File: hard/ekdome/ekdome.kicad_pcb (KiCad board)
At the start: 2 copper layers, 87 x 72 mm, 79 parts, among them J10 USB_P, J11 DBG, J20 HBS, J30 POWER, Q20 S8050, Q21 S8050, U10 CH32V203C8T6, U11 CH340E, U20 MS1192, U30 XL1509, U31 AMS1117-3.3, Y10 12M

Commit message: EK DEMO is designed. it is gone to JLC process.
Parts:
- added C100: 100nF, kicad_footprint_general:C_0603_1608Metric, F.Cu at (144.5, 129.4)
- added C25: 1uF, kicad_footprint_general:C_0603_1608Metric, F.Cu at (167.1, 133.6)
- added C26: 100nF, kicad_footprint_general:C_0603_1608Metric, F.Cu at (165.6, 133.6)
- added J21: HBS, kicad_footprint_general:PhoenixContact_MCV_1,5_2-G-3.81_1x02_P3.81mm_Vertical, F.Cu at (183.5, 118.9)
- added L31: 100mH, kicad_footprint_general:Choke_Schaffner_EE4991B-20.0x18.0mm, F.Cu at (171.0, 93.0)
- added R14: NP, kicad_footprint_general:R_0603_1608Metric, F.Cu at (122.8, 140.4)
- added R15: NP, kicad_footprint_general:R_0603_1608Metric, F.Cu at (135.0, 128.5)
- added U13: 74LVC1G86, kicad_footprint_general:SOT-23-5, F.Cu at (144.9, 126.7)
- C21, C22: value 20nF -> 22nF
- C23, C24: footprint kicad_footprint_general:C_0805_2012Metric -> kicad_footprint_general:C_1206_3216Metric
- Q20, Q21: value S8050 -> SS8050
- R12: value 330R -> 100R
- R20: value 1.6k -> 1.5k
- R21: value 3.3k -> 3k
- R40, R41, R42, R43, R44: value 10k -> 5.1k
- moved C14 88.7 mm to (112.2, 133.7), turned to 90 degrees
- moved R41 87.4 mm to (110.6, 135.3), turned to 270 degrees
- moved D21 86.7 mm to (172.7, 137.8), turned to 90 degrees
- moved R10 84.1 mm to (122.8, 138.9), turned to 180 degrees
- moved Q20 68.5 mm to (162.6, 141.6), turned to 270 degrees
- moved TP13 67.1 mm to (102.0, 139.0)
- moved D44 66.8 mm to (121.1, 122.4)
- moved C13 65.4 mm to (122.8, 137.4), turned to 180 degrees
- moved TP12 64.4 mm to (104.5, 139.0)
- moved C16 63.9 mm to (128.2, 126.9), turned to 180 degrees
- moved D22 63.9 mm to (167.3, 143.0), turned to 180 degrees
- moved C18 62.4 mm to (117.0, 110.4), turned to 180 degrees
- moved R11 61.7 mm to (132.1, 127.7), turned to 90 degrees
- moved D20 61.6 mm to (167.3, 140.6), turned to 180 degrees
- moved R31 61.3 mm to (175.0, 123.3), turned to 90 degrees
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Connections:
- net Net-(C17-Pad1) renamed /CRST
- U10 pad 10: Net-(U10-Pad10) -> /CFT
- U10 pad 14: /EN -> Net-(U10-Pad14)
- U10 pad 15: Net-(U10-Pad15) -> /EN
- U10 pad 17: Net-(U10-Pad17) -> /LRN
- U10 pad 2: Net-(U10-Pad2) -> /LPH
- U10 pad 25: Net-(U10-Pad25) -> /LPR
- U10 pad 30: /RX1 -> /TX1
- U10 pad 31: /TX1 -> /RX1
- U10 pad 37: /LRN -> Net-(U10-Pad37)
- U10 pad 38: /LPH -> /LPU
- U10 pad 39: /LPR -> Net-(U10-Pad39)
- U10 pad 40: /LPU -> Net-(U10-Pad40)
- U10 pad 44: Net-(U10-Pad44) -> /BOOT0
- U10 pad 46: /BOOT0 -> Net-(U10-Pad46)
- U20 pad 15: Net-(R25-Pad2) -> Net-(R24-Pad2)
- U20 pad 16: Net-(R24-Pad2) -> Net-(R25-Pad2)
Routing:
- net GND: track 0.00 -> 407.7 mm, vias 0 -> 112
- net VCC: track 0.00 -> 186.2 mm, vias 0 -> 7
- net /+5V: track 0.00 -> 136.4 mm, vias 0 -> 2
- net Net-(D31-Pad3): track 0.00 -> 87.8 mm
- net Net-(R14-Pad2): track 0.00 -> 72.3 mm, vias 0 -> 4
- net /VBA: track 0.00 -> 64.4 mm, vias 0 -> 2
- net Net-(D38-Pad1): track 0.00 -> 59.2 mm, vias 0 -> 2
- net /VBB: track 0.00 -> 57.6 mm, vias 0 -> 1
- net /TX2: track 0.00 -> 45.3 mm
- net /EN: track 0.00 -> 44.6 mm, vias 0 -> 2
- net /RX2: track 0.00 -> 42.3 mm, vias 0 -> 2
- net Net-(R15-Pad2): track 0.00 -> 39.2 mm, vias 0 -> 2
- net Net-(C22-Pad1): track 0.00 -> 38.8 mm, vias 0 -> 2
- net /CRST: track 0.00 -> 38.7 mm, vias 0 -> 2
- net /LPH: track 0.00 -> 38.4 mm, vias 0 -> 2
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- added copper zone on B.Cu, net GND
- added copper zone on F.Cu, net GND
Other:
- board text added: "+18V"
- board text added: "-"
- board text added: "BOOT"
- board text added: "DEC1022_1.6_HASL"
- board text added: "EKDOME_V10"
- board text added: "HBS"
- board text added: "RST"
- board text removed: "20221014_1.6_HASL"
- board text removed: "EASYPB_V11"

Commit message: V1.1 complete
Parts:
- removed D37, D38, D39: SMBJ24CA, kicad_footprint_general:D_SMB
- removed L31: 100mH, kicad_footprint_general:Choke_Schaffner_EE4991B-20.0x18.0mm
- removed R31, R32: 0R, kicad_footprint_general:R_0805_2012Metric
- added C101: 100nF, kicad_footpring_general:C_0603_1608Metric, F.Cu at (140.4, 127.9)
- added C201: NP, kicad_footpring_general:C_0603_1608Metric, F.Cu at (167.1, 137.0)
- added C27: 100nF, kicad_footpring_general:C_0603_1608Metric, F.Cu at (153.2, 126.4)
- added C28: NP, kicad_footpring_general:C_1206_3216Metric, F.Cu at (173.9, 119.3)
- added R18: 1k, kicad_footpring_general:R_0603_1608Metric, F.Cu at (141.2, 125.6)
- added R201: NP, kicad_footpring_general:R_1206_3216Metric, F.Cu at (175.1, 122.8)
- added R202: NP, kicad_footpring_general:R_1206_3216Metric, F.Cu at (172.8, 122.8)
- added R203: NP, kicad_footpring_general:R_0603_1608Metric, F.Cu at (168.7, 137.0)
- added R204: 10k, kicad_footpring_general:R_0603_1608Metric, F.Cu at (154.7, 126.4)
- added R27: 1.0R, kicad_footpring_general:R_0603_1608Metric, F.Cu at (163.4, 140.4)
- added R28: 1.0R, kicad_footpring_general:R_0603_1608Metric, F.Cu at (170.2, 134.0)
- added TL10: L, TestPoint:TestPoint_Loop_D2.50mm_Drill1.0mm, F.Cu at (176.0, 96.0)
- added TL11: L, TestPoint:TestPoint_Loop_D2.50mm_Drill1.0mm, F.Cu at (176.0, 110.0)
- added TL20: L, TestPoint:TestPoint_Loop_D2.50mm_Drill1.0mm, F.Cu at (165.0, 96.0)
- added TL21: L, TestPoint:TestPoint_Loop_D2.50mm_Drill1.0mm, F.Cu at (165.0, 110.0)
- Q20, Q21: value SS8050 -> NP
- R20: value 1.5k -> 220R
- R21: value 3k -> NP; footprint kicad_footprint_general:R_0603_1608Metric -> kicad_footpring_general:R_1206_3216Metric
- U13: footprint kicad_footprint_general:SOT-23-5 -> kicad_footpring_general:SOT-23-5
- U20: footprint kicad_footprint_general:SOIC-16_3.9x9.9mm_P1.27mm -> kicad_footpring_general:SOIC-16_3.9x9.9mm_P1.27mm
- moved R21 30.6 mm to (144.1, 98.2), turned to 90 degrees
- moved Q21 6.93 mm to (175.7, 137.3), turned to -90 degrees
- moved Q20 2.07 mm to (160.8, 140.6)
- moved C15 1.96 mm to (115.0, 122.4)
- moved R10 1.92 mm to (120.8, 138.7)
- moved R14 1.92 mm to (120.8, 140.2)
- moved C13 1.70 mm to (123.8, 138.7)
- moved C25 1.65 mm to (168.7, 133.1)
- moved C26 1.65 mm to (167.2, 133.1)
- moved C24 1.48 mm to (167.3, 139.7)
- moved D20 1.48 mm to (167.3, 142.1)
- moved D22 1.48 mm to (167.3, 144.5)
- moved R13 0.96 mm to (118.0, 122.4), turned to 180 degrees
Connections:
- C13 pad 1: GND -> VCC
- C13 pad 2: VCC -> GND
- C30 pad 1: Net-(C30-Pad1) -> /VHH
- C32 pad 1: Net-(C30-Pad1) -> /VHH
- D32 pad 1: Net-(C30-Pad1) -> /VHH
- J10 pad A5: Net-(J10-PadA5) -> unconnected-(J10-PadA5)
- J10 pad B5: Net-(J10-PadB5) -> unconnected-(J10-PadB5)
- J11 pad A5: Net-(J11-PadA5) -> unconnected-(J11-PadA5)
- J11 pad B5: Net-(J11-PadB5) -> unconnected-(J11-PadB5)
- R20 pad 2: /RX2 -> /RX3
- R21 pad 1: GND -> Net-(R21-Pad1)
- R21 pad 2: /RX2 -> /VHH
- R23 pad 2: /TX2 -> /TX3
- R30 pad 2: Net-(C30-Pad1) -> /VHH
- U10 pad 11: Net-(U10-Pad11) -> unconnected-(U10-Pad11)
- U10 pad 14: Net-(U10-Pad14) -> unconnected-(U10-Pad14)
- U10 pad 16: Net-(U10-Pad16) -> unconnected-(U10-Pad16)
- U10 pad 26: Net-(U10-Pad26) -> unconnected-(U10-Pad26)
- U10 pad 27: Net-(U10-Pad27) -> unconnected-(U10-Pad27)
- U10 pad 28: Net-(U10-Pad28) -> unconnected-(U10-Pad28)
- U10 pad 29: Net-(U10-Pad29) -> unconnected-(U10-Pad29)
- U10 pad 3: Net-(U10-Pad3) -> unconnected-(U10-Pad3)
- U10 pad 34: Net-(U10-Pad34) -> unconnected-(U10-Pad34)
- U10 pad 37: Net-(U10-Pad37) -> unconnected-(U10-Pad37)
- U10 pad 39: Net-(U10-Pad39) -> unconnected-(U10-Pad39)
- U10 pad 4: Net-(U10-Pad4) -> unconnected-(U10-Pad4)
- U10 pad 40: Net-(U10-Pad40) -> unconnected-(U10-Pad40)
- U10 pad 41: Net-(U10-Pad41) -> unconnected-(U10-Pad41)
- U10 pad 42: Net-(U10-Pad42) -> unconnected-(U10-Pad42)
- U10 pad 43: Net-(U10-Pad43) -> unconnected-(U10-Pad43)
- U10 pad 45: Net-(U10-Pad45) -> unconnected-(U10-Pad45)
- U10 pad 46: Net-(U10-Pad46) -> unconnected-(U10-Pad46)
- U10 pad 47: VCC -> GND
- U10 pad 48: GND -> VCC
- U11 pad 5: Net-(U11-Pad5) -> unconnected-(U11-Pad5)
- U13 pad 1: /TX2 -> /TX3
- U13 pad 2: /RX2 -> /RX3
- U13 pad 4: /CFT -> Net-(R18-Pad1)
- U20 pad 12: GND -> /CLB
- U20 pad 14: GND -> /CLA
- U20 pad 2: Net-(U20-Pad2) -> Net-(R21-Pad1)
- U20 pad 7: Net-(Q20-Pad1) -> Net-(Q21-Pad1)
- U20 pad 8: Net-(Q21-Pad1) -> Net-(Q20-Pad1)
- U30 pad 1: Net-(C30-Pad1) -> /VHH
- U30 pad 4: Net-(U30-Pad4) -> unconnected-(U30-Pad4)
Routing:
- net Net-(D31-Pad3): track 87.8 -> 22.7 mm
- net Net-(D38-Pad1): track 59.2 -> 0.00 mm, vias 2 -> 0
- net /TX3: track 0.00 -> 49.8 mm, vias 0 -> 2
- net /TX2: track 45.3 -> 0.00 mm
- net /RX3: track 0.00 -> 44.9 mm, vias 0 -> 4
- net Net-(R21-Pad1): track 0.00 -> 42.7 mm, vias 0 -> 2
- net /RX2: track 42.3 -> 0.00 mm, vias 2 -> 0
- net /VHH: track 0.00 -> 42.2 mm, vias 0 -> 2
- net Net-(C30-Pad1): track 34.4 -> 0.00 mm
- net Net-(D37-Pad1): track 33.6 -> 0.00 mm, vias 2 -> 0
- net Net-(C21-Pad1): track 35.3 -> 54.9 mm
- net Net-(C22-Pad1): track 38.8 -> 56.0 mm
- net /CLA: track 0.00 -> 14.4 mm, vias 0 -> 2
- net /+5V: track 136.4 -> 148.5 mm, vias 2 -> 3
- net VCC: track 186.2 -> 197.7 mm
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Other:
- net class Default removed
- board text added: "EKDEMO_V11"
- board text added: "JUN0923_1.6_HASL"
- board text removed: "DEC1022_1.6_HASL"
- board text removed: "EKDOME_V10"

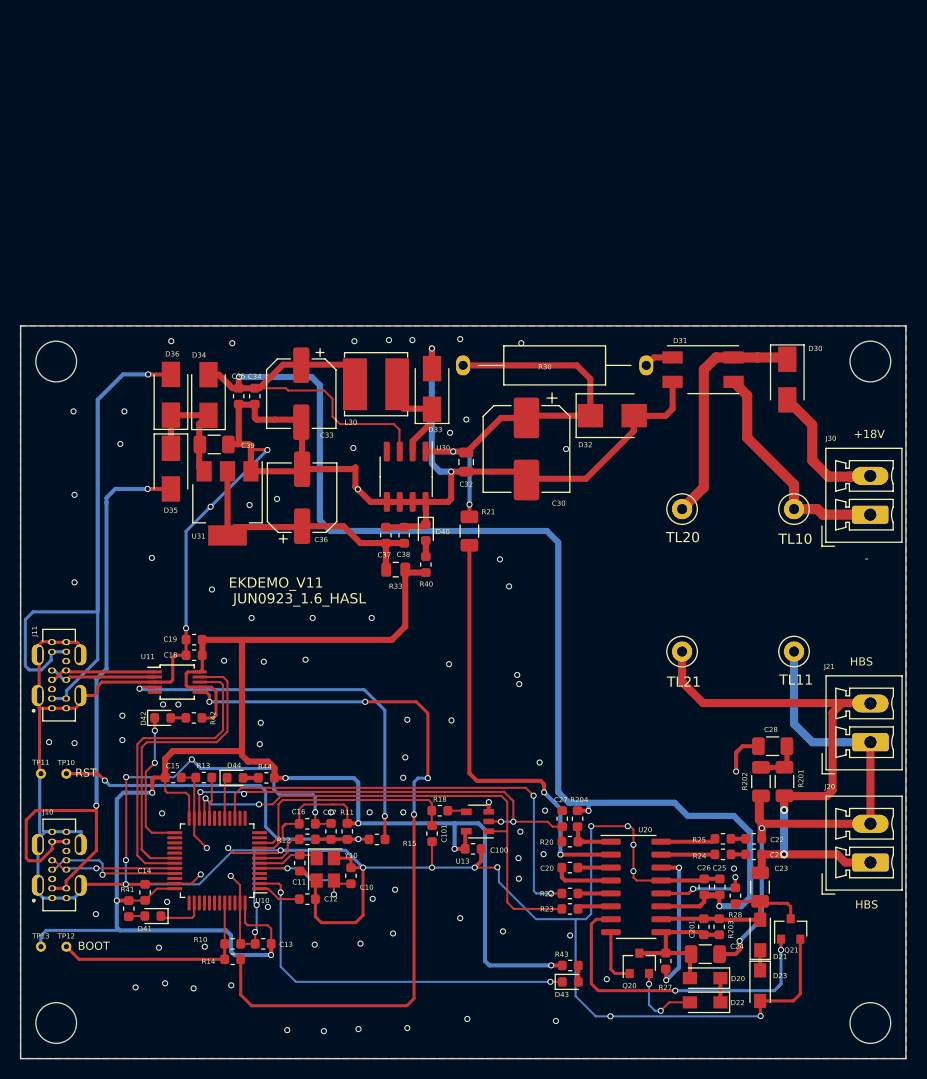
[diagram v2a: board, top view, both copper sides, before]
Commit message: 增加485端口用于协议调试
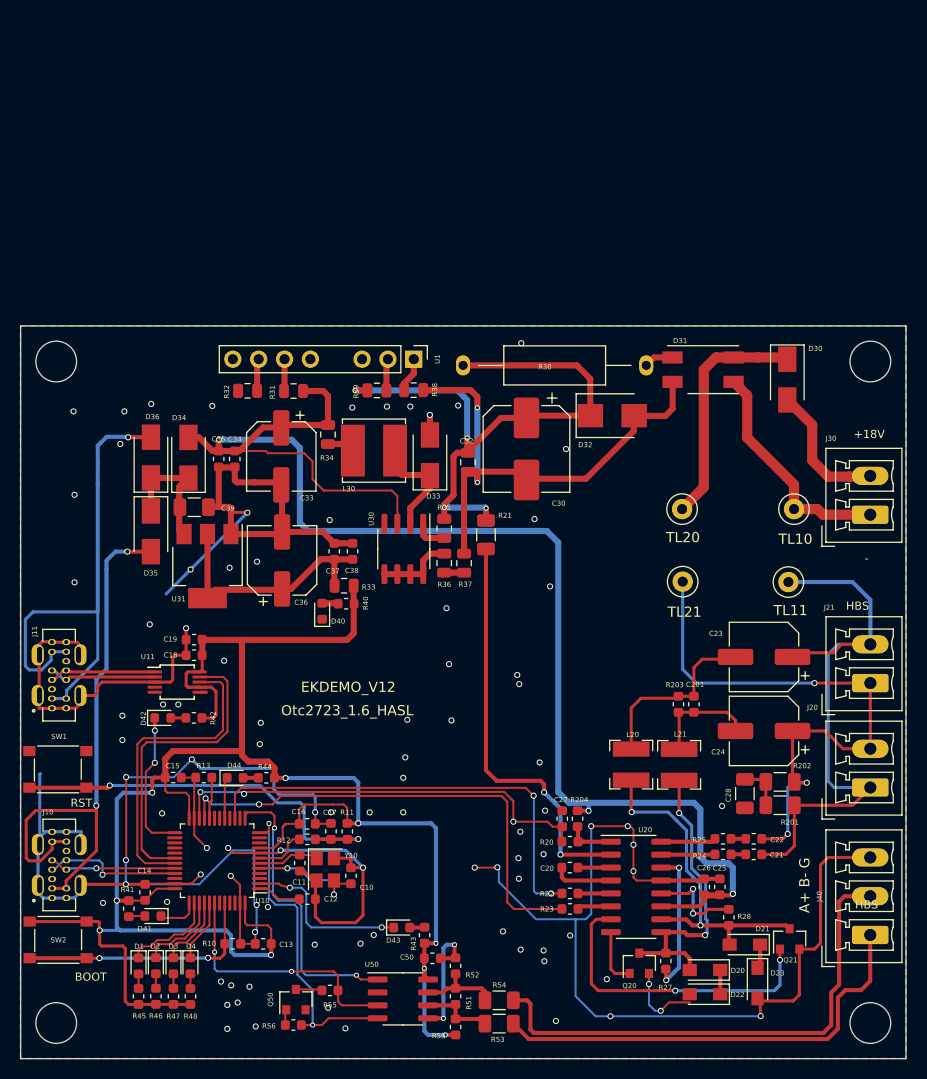
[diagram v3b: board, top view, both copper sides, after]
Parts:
- removed C101: 100nF, kicad_footpring_general:C_0603_1608Metric
- removed R14, R15: NP, kicad_footprint_general:R_0603_1608Metric
- removed R18: 1k, kicad_footpring_general:R_0603_1608Metric
- removed TP10: NRST, kicad_footprint_general:TestPoint_THTPad_D1.0mm_Drill0.5mm
- removed TP11: GND, kicad_footprint_general:TestPoint_THTPad_D1.0mm_Drill0.5mm
- removed TP12: BOOT, kicad_footprint_general:TestPoint_THTPad_D1.0mm_Drill0.5mm
- removed TP13: VCC, kicad_footprint_general:TestPoint_THTPad_D1.0mm_Drill0.5mm
- removed U13: 74LVC1G86, kicad_footpring_general:SOT-23-5
- added D1: RED, kicad_footprint_general:LED_0603_1608Metric, F.Cu at (111.6, 140.9)
- added D2: RED, kicad_footprint_general:LED_0603_1608Metric, F.Cu at (113.3, 140.9)
- added D3: RED, kicad_footprint_general:LED_0603_1608Metric, F.Cu at (115.0, 140.9)
- added D4: RED, kicad_footprint_general:LED_0603_1608Metric, F.Cu at (116.7, 140.9)
- added J40: RS485, kicad_footprint_general:PhoenixContact_MCV_1,5_3-G-3.81_1x03_P3.81mm_Vertical, F.Cu at (183.5, 137.8)
- added L20: 330uH, Inductor_SMD:L_Bourns-SRN4018, F.Cu at (160.0, 121.1)
- added L21: 330uH, Inductor_SMD:L_Bourns-SRN4018, F.Cu at (164.7, 121.1)
- added Q50: SS8050, kicad_footprint_general:SOT-23, F.Cu at (127.0, 144.2)
- added R31: 0R, kicad_footprint_general:R_0805_2012Metric, F.Cu at (126.8, 84.4)
- added R32: 0R, kicad_footprint_general:R_0805_2012Metric, F.Cu at (122.3, 84.4)
- added R34: NP, kicad_footprint_general:R_0805_2012Metric, F.Cu at (130.2, 88.7)
- added R35: NP, kicad_footprint_general:R_0805_2012Metric, F.Cu at (141.6, 97.9)
- added R36: NP, kicad_footprint_general:R_0805_2012Metric, F.Cu at (141.6, 101.3)
- added R37: NP, kicad_footprint_general:R_0805_2012Metric, F.Cu at (143.6, 101.3)
- added R38: 0R, kicad_footprint_general:R_0805_2012Metric, F.Cu at (138.6, 84.3)
- added R39: 0R, kicad_footprint_general:R_0805_2012Metric, F.Cu at (135.0, 84.3)
- added R45: 5.1k, kicad_footprint_general:R_0603_1608Metric, F.Cu at (111.6, 143.9)
- added R46: 5.1k, kicad_footprint_general:R_0603_1608Metric, F.Cu at (113.3, 143.9)
- added R47: 5.1k, kicad_footprint_general:R_0603_1608Metric, F.Cu at (115.0, 143.9)
- added R48: 5.1k, kicad_footprint_general:R_0603_1608Metric, F.Cu at (116.7, 143.9)
- added R50: 4.7k, kicad_footprint_general:R_0603_1608Metric, F.Cu at (142.7, 146.9)
- added R51: NP, kicad_footprint_general:R_0603_1608Metric, F.Cu at (142.7, 143.9)
- added R52: 4.7k, kicad_footprint_general:R_0603_1608Metric, F.Cu at (142.7, 140.9)
- added R53: 10R, kicad_footprint_general:R_1206_3216Metric, F.Cu at (147.0, 146.6)
- added R54: 10R, kicad_footprint_general:R_1206_3216Metric, F.Cu at (147.0, 144.3)
- added R55: 1k, kicad_footprint_general:R_0603_1608Metric, F.Cu at (130.4, 143.3)
- added R56: 4.7k, kicad_footprint_general:R_0603_1608Metric, F.Cu at (126.8, 146.7)
- added SW1: RST, kicad_footprint_general:SW_KAN0541, F.Cu at (103.7, 121.6)
- added SW2: RST, kicad_footprint_general:SW_KAN0541, F.Cu at (103.7, 138.3)
- added U1: DCDC_SIP8, kicad_footprint_general:TDKSIP8, F.Cu at (138.6, 81.3)
- added U50: SP3485CN, kicad_footprint_general:SOIC-8_3.9x4.9mm_P1.27mm, F.Cu at (137.6, 144.1)
- C23, C24: value 10uF -> 22uF; footprint kicad_footprint_general:C_1206_3216Metric -> kicad_footprint_general:CP_Elec_6.3x5.4
- moved C24 22.7 mm to (173.1, 117.8)
- moved C23 22.6 mm to (173.1, 110.5), turned to 180 degrees
- moved R203 22.2 mm to (164.6, 115.2)
- moved C201 21.9 mm to (166.2, 115.2)
- moved D43 17.4 mm to (137.4, 137.1)
- moved R43 14.6 mm to (139.7, 137.9), turned to 90 degrees
- moved D40 12.8 mm to (129.6, 106.0), turned to 90 degrees
- moved C50 11.5 mm to (140.5, 140.1)
- moved R40 8.73 mm to (132.0, 105.3), turned to 180 degrees
- moved J20 7.37 mm to (183.5, 123.4)
- moved U30 7.10 mm to (137.7, 99.9)
- moved TL21 6.87 mm to (165.1, 103.1)
- moved TL11 6.85 mm to (175.4, 103.2)
- moved D33 6.53 mm to (140.2, 90.7)
- moved L30 6.53 mm to (134.7, 90.3)
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- renumbered C100 to C50
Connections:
- C21 pad 1: Net-(C21-Pad1) -> Net-(J20-Pin_1)
- C22 pad 1: Net-(C22-Pad1) -> Net-(J20-Pin_2)
- C23 pad 1: Net-(C21-Pad1) -> Net-(J20-Pin_1)
- C24 pad 1: Net-(C22-Pad1) -> Net-(J20-Pin_2)
- C30 pad 2: GND -> Net-(D31--)
- C32 pad 2: GND -> Net-(D31--)
- D20 pad 2: Net-(C201-Pad2) -> Net-(D20-A2)
- D21 pad 2: Net-(C201-Pad1) -> Net-(D21-A2)
- D31 pad 2: GND -> Net-(D31--)
- D32 pad 2: GND -> Net-(D31--)
- J20 pad 1: Net-(C21-Pad1) -> Net-(J20-Pin_1)
- J20 pad 2: Net-(C22-Pad1) -> Net-(J20-Pin_2)
- J21 pad 1: Net-(C22-Pad1) -> Net-(J20-Pin_2)
- J21 pad 2: Net-(C21-Pad1) -> Net-(J20-Pin_1)
- L30 pad 1: /+5V -> Net-(L30-Pad1)
- Q20 pad 3: Net-(C201-Pad2) -> Net-(D20-A2)
- Q21 pad 3: Net-(C201-Pad1) -> Net-(D21-A2)
- R201 pad 1: Net-(C21-Pad1) -> Net-(J20-Pin_1)
- R202 pad 1: Net-(C22-Pad1) -> Net-(J20-Pin_2)
- R27 pad 1: Net-(C201-Pad2) -> Net-(D20-A2)
- R28 pad 1: Net-(C201-Pad1) -> Net-(D21-A2)
- TL11 pad 1: Net-(C22-Pad1) -> Net-(J20-Pin_1)
- TL21 pad 1: Net-(C21-Pad1) -> Net-(J20-Pin_2)
- U10 pad 37: unconnected-(U10-Pad37) -> /LPU
- U10 pad 38: /LPU -> /LD1
- U10 pad 39: unconnected-(U10-Pad39) -> /LD2
- U10 pad 40: unconnected-(U10-Pad40) -> /LD3
- U10 pad 41: unconnected-(U10-Pad41) -> /LD4
- U10 pad 42: unconnected-(U10-Pad42) -> /SLT
- U11 pad 4: Net-(R15-Pad2) -> unconnected-(U11-RTS-Pad4)
- U11 pad 6: Net-(R14-Pad2) -> unconnected-(U11-TNOW-Pad6)
- U20 pad 10: Net-(C201-Pad1) -> Net-(D21-A2)
- U20 pad 9: Net-(C201-Pad2) -> Net-(D20-A2)
- U30 pad 1: /VHH -> Net-(U30-VIN)
- U30 pad 5: GND -> Net-(R36-Pad1)
- U30 pad 6: GND -> Net-(R36-Pad1)
- U30 pad 7: GND -> Net-(R36-Pad1)
- U30 pad 8: GND -> Net-(R36-Pad1)
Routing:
- net Net-(R14-Pad2): track 74.1 -> 0.00 mm, vias 4 -> 0
- net GND: track 416.8 -> 344.2 mm, vias 110 -> 96
- net Net-(J20-Pin_1): track 0.00 -> 58.5 mm
- net Net-(J20-Pin_2): track 0.00 -> 58.2 mm, vias 0 -> 3
- net Net-(C22-Pad1): track 56.0 -> 0.00 mm, vias 2 -> 0
- net Net-(C21-Pad1): track 54.9 -> 0.00 mm, vias 2 -> 0
- net Net-(D31--): track 0.00 -> 51.4 mm, vias 0 -> 2
- net /SB: track 0.00 -> 50.1 mm
- net /SA: track 0.00 -> 44.4 mm
- net Net-(R15-Pad2): track 39.2 -> 0.00 mm, vias 2 -> 0
- net Net-(D21-A2): track 0.00 -> 34.3 mm, vias 0 -> 2
- net /TX2: track 0.00 -> 32.2 mm, vias 0 -> 2
- net Net-(D20-A2): track 0.00 -> 29.6 mm, vias 0 -> 2
- net /RX2: track 0.00 -> 29.2 mm, vias 0 -> 2
- net /SLT: track 0.00 -> 25.5 mm, vias 0 -> 2
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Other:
- board text added: "A+ B- G"
- board text added: "EKDEMO_V12"
- board text added: "Otc2723_1.6_HASL"
- board text removed: "EKDEMO_V11"
- board text removed: "JUN0923_1.6_HASL"
